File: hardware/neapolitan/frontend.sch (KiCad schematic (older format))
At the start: 144 parts, among them J10 GND_CLIP, J2 RF-SHIELD-FRAME, J3 RF-SHIELD-COVER, J4 MOUNTING_HOLE, J5 MOUNTING_HOLE, J6 MOUNTING_HOLE, J7 MOUNTING_HOLE, J8 MOUNTING_HOLE, J9 MOUNTING_HOLE, P13 GPO1, P17 GPO6, P19 GPO3, P21 REF_IN, P27 MIXER_SDATA, P31 MIXER_SCLK, P32 MIXER_ENX, P33 MIXER_RESETX, P34 MIX_BYPASS, P35 !MIX_BYPASS, P4 ANTENNA, P42 TX, P43 RX, P44 HP, P45 LP, P46 TX_MIX_BP, P47 RX_MIX_BP, P48 TX_AMP, P49 RX_AMP, P50 AMP_BYPASS, P51 !TX_AMP_PWR, P52 !RX_AMP_PWR, P6 GPO4, P7 GPO2, Q1 MOSFET_P, Q2 MOSFET_P, Q4 MOSFET_P, T1 MIX_IN_BALUN, T2 MIX_OUT_BALUN, U1 SKY13350, U10 SKY13350, U11 SKY13350, U12 SKY13317, U13 MGA-81563, U14 SKY13317, U2 SKY13350, U25 MGA-81563, U3 RX_LOWPASS_FILTER, U4 RFFC5072, U5 SKY13350, U6 SKY13350, U7 SKY13350, U8 RX_HIGHPASS_FILTER, U9 SKY13317

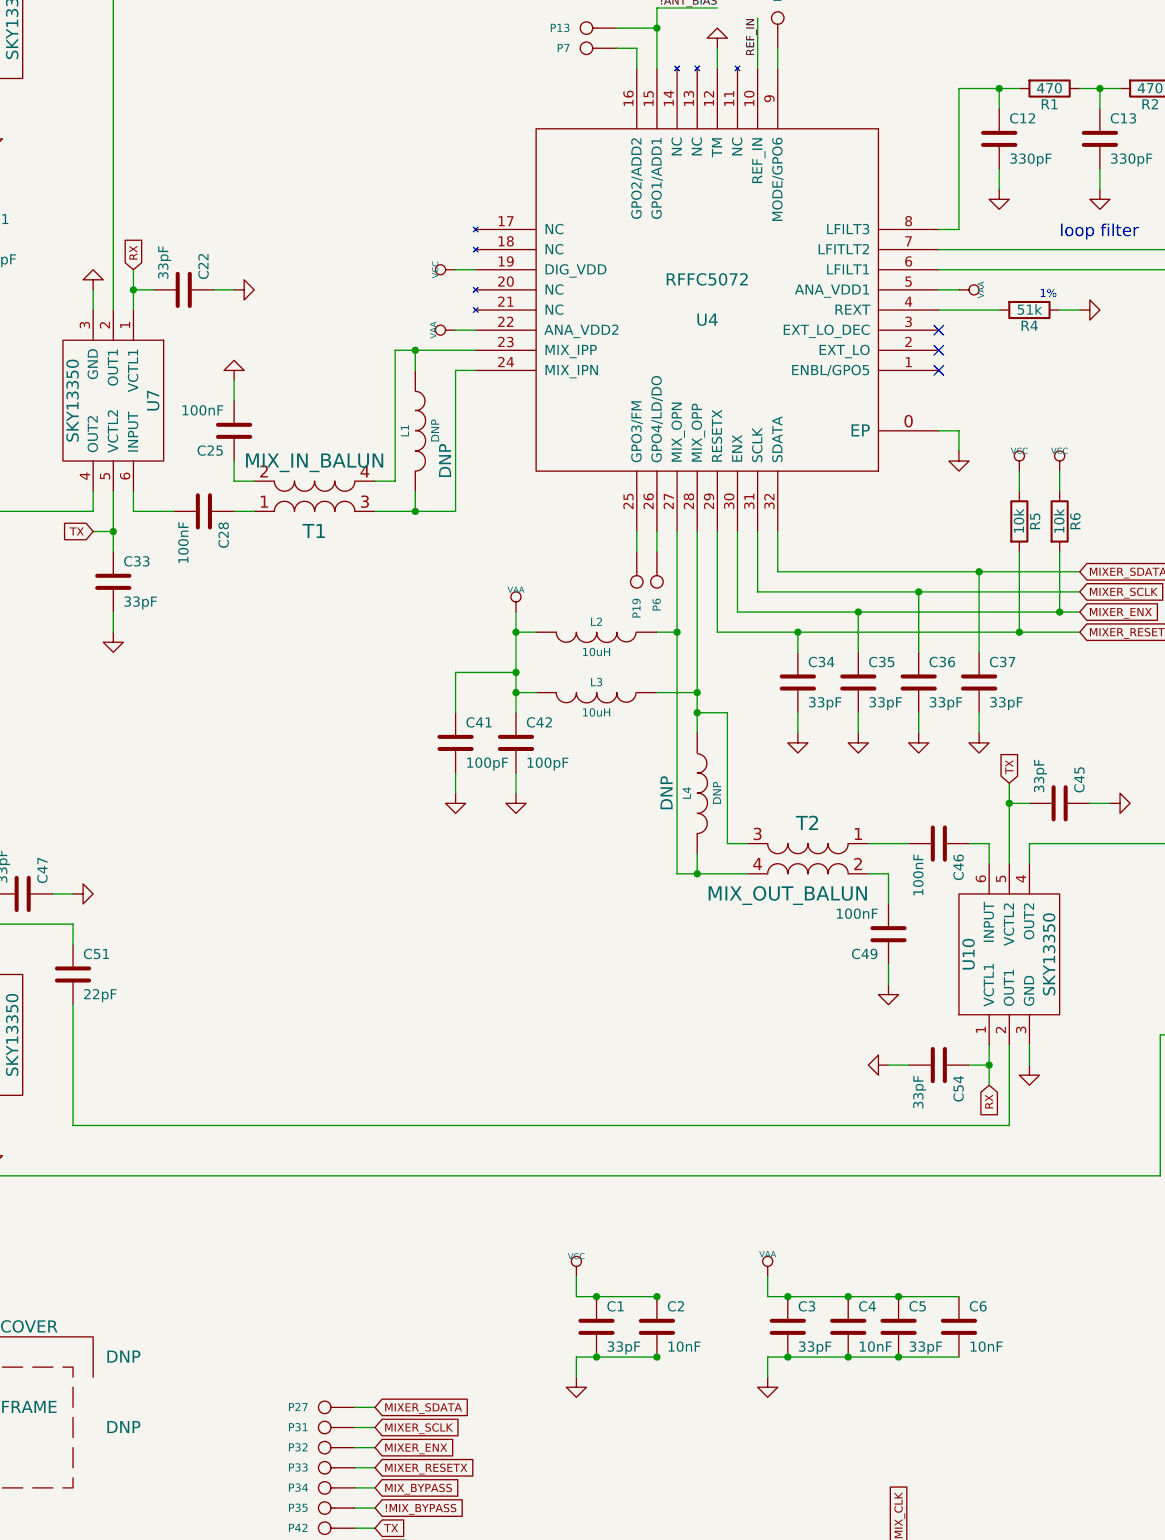
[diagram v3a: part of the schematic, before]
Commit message: Neapolitan: added RF chokes to some supply pins as a noise reduction experiment
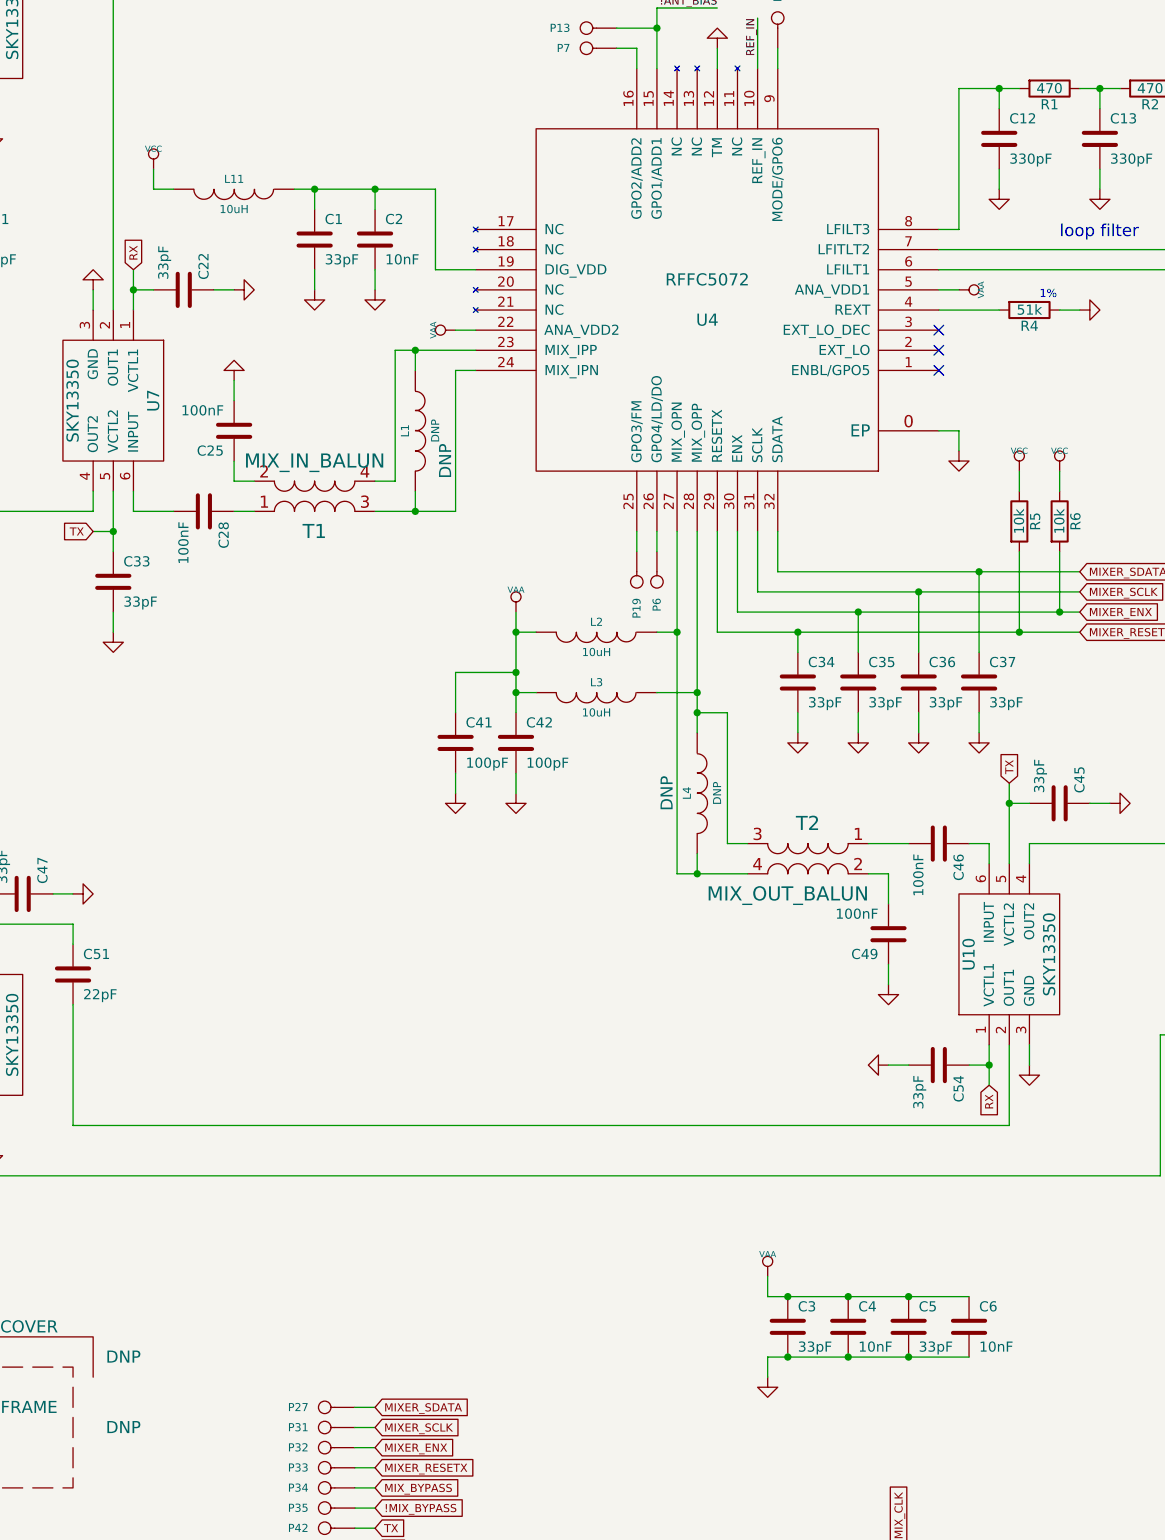
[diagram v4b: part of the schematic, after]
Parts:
- added L11: 10uH, hackrf:GSG-0603, symbol INDUCTOR
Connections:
- net VCC: now also L11.2; no longer C1.1, C2.1, U4.19 (DIG_VDD)
- new net: C1.1, C2.1, L11.1, U4.19 (DIG_VDD)
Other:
- moved on the sheet: C1, C2, C5, C6

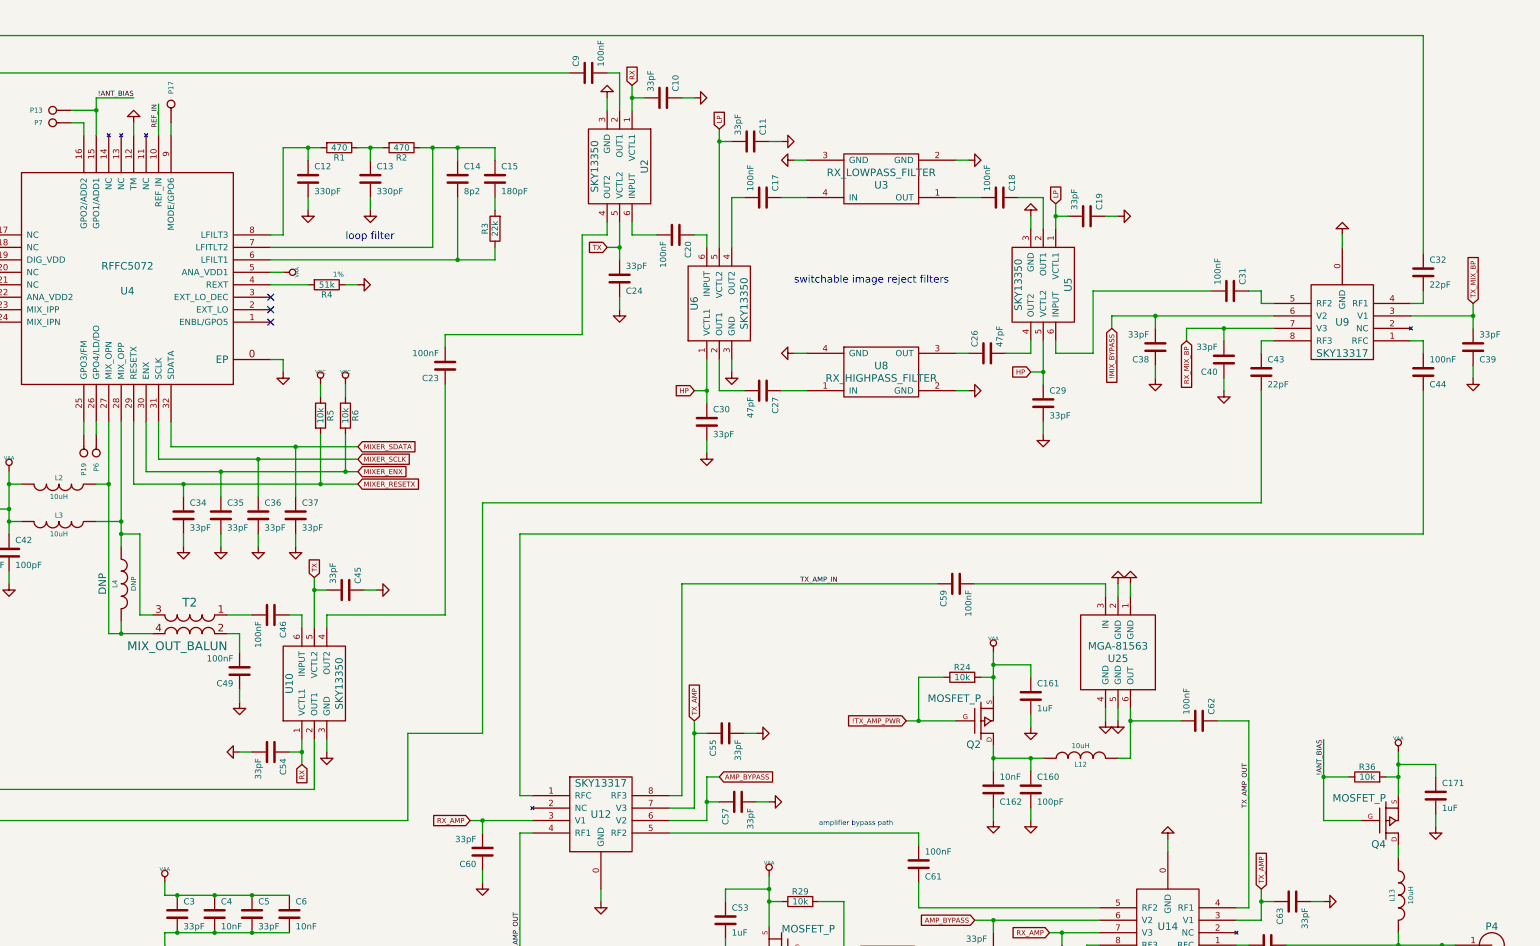
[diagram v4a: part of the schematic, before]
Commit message: Neapolitan: replaced antenna port power MOSFET with current limited power switch
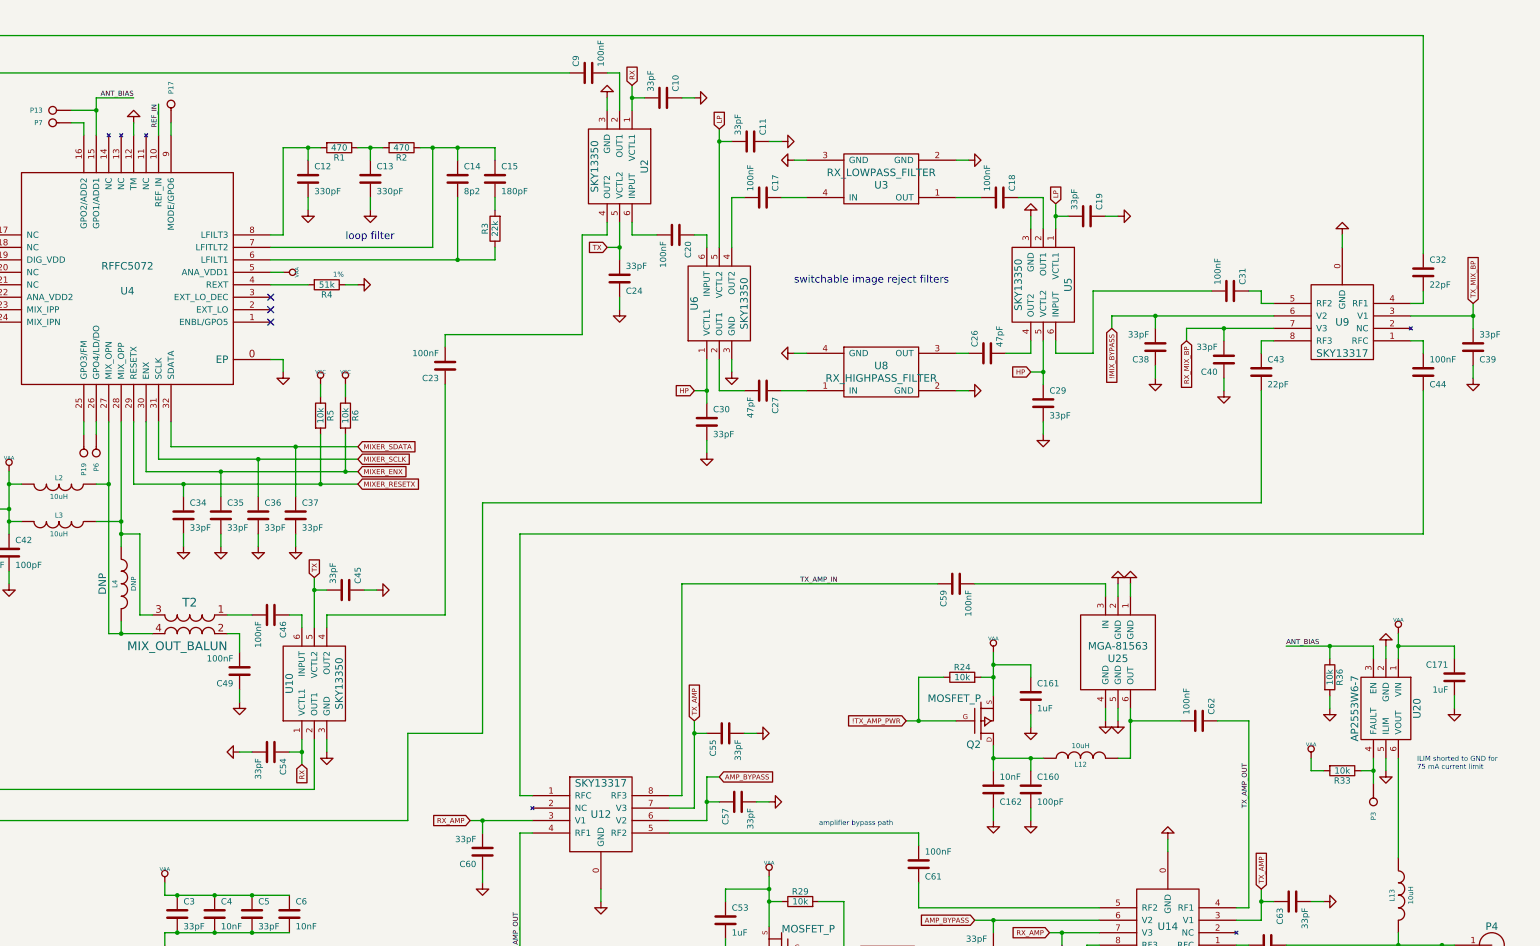
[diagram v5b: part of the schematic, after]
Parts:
- removed Q4: MOSFET_P, gsg-modules:SOT23GDS, symbol MOSFET_P
- added P3: ANT_FAULT, hackrf:GSG-TESTPOINT-50MIL, symbol CONN_1
- added R33: 10k, hackrf:GSG-0402, symbol R
- added U20: AP2553W6-7, gsg-modules:SOT457, symbol NX5P2553GV
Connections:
- net GND: now also R36.2, U20.2 (GND), U20.5 (ILIM)
- net VAA: now also R33.2, U20.1 (VIN); no longer R36.2
- net at L13.1: now also U20.6 (VOUT)
- net !ANT_BIAS renamed ANT_BIAS
- net ANT_BIAS: now also U20.3 (EN)
- new net: P3.1, R33.1, U20.4 (FAULT)
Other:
- note added: "ILIM shorted to GND for\n75 mA current limit"
- moved on the sheet: C171, R36
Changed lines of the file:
@@
 Wire Wire Line
 	16300 8850 16300 8950
-Connection ~ 15550 7100
-Wire Wire Line
-	15550 7100 15450 7100
-Wire Wire Line
-	15850 7100 15850 7000
-Wire Wire Line
-	15850 7500 15850 7400
-Wire Wire Line
-	15550 6900 15550 7250
-Connection ~ 15550 7000
-Wire Wire Line
-	15150 7100 14950 7100
-Wire Wire Line
-	14950 6800 14950 7450
-Wire Wire Line
-	15850 7000 15550 7000
 $Comp
 L VAA #PWR089
 U 1 1 52EA1171
-P 15550 6900
-F 0 "#PWR089" H 15550 6960 30  0001 C CNN
-F 1 "VAA" H 15550 7010 30  0000 C CNN
-F 2 "" H 15550 6900 60  0001 C CNN
-F 3 "" H 15550 6900 60  0001 C CNN
-	1    15550 6900
+P 15550 5950
+F 0 "#PWR089" H 15550 6010 30  0001 C CNN
+F 1 "VAA" H 15550 6060 30  0000 C CNN
+F 2 "" H 15550 5950 60  0001 C CNN
+F 3 "" H 15550 5950 60  0001 C CNN
+	1    15550 5950
 	1    0    0    -1
 $EndComp
@@
 L GND #PWR090
 U 1 1 52EA1177
-P 15850 7500
-F 0 "#PWR090" H 15850 7500 30  0001 C CNN
-F 1 "GND" H 15850 7430 30  0001 C CNN
-F 2 "" H 15850 7500 60  0001 C CNN
-F 3 "" H 15850 7500 60  0001 C CNN
-	1    15850 7500
+P 16000 6550
+F 0 "#PWR090" H 16000 6550 30  0001 C CNN
+F 1 "GND" H 16000 6480 30  0001 C CNN
+F 2 "" H 16000 6550 60  0001 C CNN
+F 3 "" H 16000 6550 60  0001 C CNN
+	1    16000 6550
 	1    0    0    -1
 $EndComp
@@
 L R R36
 U 1 1 52EA1180
-P 15300 7100
-F 0 "R36" V 15380 7100 50  0000 C CNN
-F 1 "10k" V 15300 7100 50  0000 C CNN
-F 2 "hackrf:GSG-0402" H 15300 7100 60  0001 C CNN
-F 3 "" H 15300 7100 60  0001 C CNN
-F 4 "Stackpole" H 15300 7100 60  0001 C CNN "Manufacturer"
-F 5 "RMCF0402JT10K0" H 15300 7100 60  0001 C CNN "Part Number"
-F 6 "RES 10K OHM 1/16W 5% 0402 SMD" H 15300 7100 60  0001 C CNN "Description"
-	1    15300 7100
-	0    -1   -1   0
+P 15000 6300
+F 0 "R36" V 15080 6300 50  0000 C CNN
+F 1 "10k" V 15000 6300 50  0000 C CNN
+F 2 "hackrf:GSG-0402" H 15000 6300 60  0001 C CNN
+F 3 "" H 15000 6300 60  0001 C CNN
+F 4 "Stackpole" H 15000 6300 60  0001 C CNN "Manufacturer"
+F 5 "RMCF0402JT10K0" H 15000 6300 60  0001 C CNN "Part Number"
+F 6 "RES 10K OHM 1/16W 5% 0402 SMD" H 15000 6300 60  0001 C CNN "Description"
+	1    15000 6300
+	1    0    0    -1
 $EndComp
 $Comp
@@
 L C C171
 U 1 1 52EA119B
-P 15850 7250
-F 0 "C171" H 15900 7350 50  0000 L CNN
-F 1 "1uF" H 15900 7150 50  0000 L CNN
-F 2 "hackrf:GSG-0402" H 15850 7250 60  0001 C CNN
-F 3 "" H 15850 7250 60  0001 C CNN
-F 4 "Taiyo Yuden" H 15850 7250 60  0001 C CNN "Manufacturer"
-F 5 "LMK105BJ105KV-F" H 15850 7250 60  0001 C CNN "Part Number"
-F 6 "CAP CER 1UF 10V 10% X5R 0402" H 15850 7250 60  0001 C CNN "Description"
-	1    15850 7250
-	1    0    0    -1
-$EndComp
-$Comp
-L MOSFET_P Q4
-U 1 1 52EA11B0
-P 15450 7450
-F 0 "Q4" H 15450 7640 60  0000 R CNN
-F 1 "MOSFET_P" H 15450 7270 60  0000 R CNN
-F 2 "gsg-modules:SOT23GDS" H 15450 7450 60  0001 C CNN
-F 3 "" H 15450 7450 60  0001 C CNN
-F 4 "Fairchild" H 15450 7450 60  0001 C CNN "Manufacturer"
-F 5 "BSS84" H 15450 7450 60  0001 C CNN "Part Number"
-F 6 "MOSFET P-CH 50V 130MA SOT-23" H 15450 7450 60  0001 C CNN "Description"
-	1    15450 7450
-	1    0    0    1
+P 16000 6300
+F 0 "C171" H 16050 6400 50  0000 L CNN
+F 1 "1uF" H 16050 6200 50  0000 L CNN
+F 2 "hackrf:GSG-0402" H 16000 6300 60  0001 C CNN
+F 3 "" H 16000 6300 60  0001 C CNN
+F 4 "Taiyo Yuden" H 16000 6300 60  0001 C CNN "Manufacturer"
+F 5 "LMK105BJ105KV-F" H 16000 6300 60  0001 C CNN "Part Number"
+F 6 "CAP CER 1UF 10V 10% X5R 0402" H 16000 6300 60  0001 C CNN "Description"
+	1    16000 6300
+	-1   0    0    -1
 $EndComp
 Wire Wire Line
@@
 Connection ~ 15550 8450
 Wire Wire Line
-	14950 7450 15250 7450
-Connection ~ 14950 7100
-Wire Wire Line
-	15550 7650 15550 7750
+	15550 6950 15550 7750
 Wire Wire Line
 	5000 1850 4900 1850
@@
 Connection ~ 5100 1750
 Text Label 5400 1650 2    40   ~ 0
-!ANT_BIAS
+ANT_BIAS
 Wire Wire Line
 	5100 1650 5400 1650
-Text Label 14950 6800 3    40   ~ 0
-!ANT_BIAS
+Text Label 14650 6050 0    40   ~ 0
+ANT_BIAS
 Wire Wire Line
 	15650 3400 16150 3400
@@
 	4000 2950 4000 2550
 Connection ~ 3700 2550
+$Comp
+L NX5P2553GV U20
+U 1 1 57E6AE8D
+P 15450 6550
+F 0 "U20" H 15450 6800 60  0000 C CNN
+F 1 "AP2553W6-7" H 15450 6300 60  0000 C CNN
+F 2 "gsg-modules:SOT457" H 15450 6550 60  0001 C CNN
+F 3 "" H 15450 6550 60  0000 C CNN
+F 4 "Diodes Inc." H 15450 6550 60  0001 C CNN "Manufacturer"
+F 5 "AP2553W6-7" H 15450 6550 60  0001 C CNN "Part Number"
+F 6 "IC PD SW CURR LIMIT SOT26" H 15450 6550 60  0001 C CNN "Description"
+	1    15450 6550
+	0    1    1    0
+$EndComp
+$Comp
+L GND #PWR092
+U 1 1 57E6B2C6
+P 15450 6050
+F 0 "#PWR092" H 15450 6050 30  0001 C CNN
+F 1 "GND" H 15450 5980 30  0001 C CNN
+F 2 "" H 15450 6050 60  0001 C CNN
+F 3 "" H 15450 6050 60  0001 C CNN
+	1    15450 6050
+	-1   0    0    1
+$EndComp
+$Comp
+L GND #PWR093
+U 1 1 57E6CFB6
+P 15000 6550
+F 0 "#PWR093" H 15000 6550 30  0001 C CNN
+F 1 "GND" H 15000 6480 30  0001 C CNN
+F 2 "" H 15000 6550 60  0001 C CNN
+F 3 "" H 15000 6550 60  0001 C CNN
+	1    15000 6550
+	1    0    0    -1
+$EndComp
+Wire Wire Line
+	15000 6450 15000 6550
+Wire Wire Line
+	14650 6050 15350 6050
+Wire Wire Line
+	15000 6050 15000 6150
+Connection ~ 15000 6050
+$Comp
+L R R33
+U 1 1 57E6E64A
+P 15100 7050
+F 0 "R33" V 15180 7050 50  0000 C CNN
+F 1 "10k" V 15100 7050 50  0000 C CNN
+F 2 "hackrf:GSG-0402" H 15100 7050 60  0001 C CNN
+F 3 "" H 15100 7050 60  0001 C CNN
+F 4 "Stackpole" H 15100 7050 60  0001 C CNN "Manufacturer"
+F 5 "RMCF0402JT10K0" H 15100 7050 60  0001 C CNN "Part Number"
+F 6 "RES 10K OHM 1/16W 5% 0402 SMD" H 15100 7050 60  0001 C CNN "Description"
+	1    15100 7050
+	0    1    1    0
+$EndComp
+$Comp
+L GND #PWR094
+U 1 1 57E70C91
+P 15450 7050
+F 0 "#PWR094" H 15450 7050 30  0001 C CNN
+F 1 "GND" H 15450 6980 30  0001 C CNN
+F 2 "" H 15450 7050 60  0001 C CNN
+F 3 "" H 15450 7050 60  0001 C CNN
+	1    15450 7050
+	1    0    0    -1
+$EndComp
+Wire Wire Line
+	15450 7050 15450 6950
+Wire Wire Line
+	15550 5950 15550 6150
+Wire Wire Line
+	15550 6050 16000 6050
+Wire Wire Line
+	16000 6050 16000 6150
+Connection ~ 15550 6050
+Wire Wire Line
+	16000 6450 16000 6550
+Wire Wire Line
+	15450 6050 15450 6150
+Wire Wire Line
+	15350 6050 15350 6150
+$Comp
+L VAA #PWR095
+U 1 1 57E75398
+P 14850 6950
+F 0 "#PWR095" H 14850 7010 30  0001 C CNN
+F 1 "VAA" H 14850 7060 30  0000 C CNN
+F 2 "" H 14850 6950 60  0001 C CNN
+F 3 "" H 14850 6950 60  0001 C CNN
+	1    14850 6950
+	1    0    0    -1
+$EndComp
+Wire Wire Line
+	14850 6950 14850 7050
+Wire Wire Line
+	14850 7050 14950 7050
+Wire Wire Line
+	15250 7050 15350 7050
+Wire Wire Line
+	15350 6950 15350 7150
+$Comp
+L CONN_1 P3
+U 1 1 57E76694
+P 15350 7300
+F 0 "P3" H 15430 7300 40  0000 L CNN
+F 1 "ANT_FAULT" H 15350 7355 30  0001 C CNN
+F 2 "hackrf:GSG-TESTPOINT-50MIL" H 15350 7300 60  0001 C CNN
+F 3 "" H 15350 7300 60  0001 C CNN
+F 4 "DNP" H 15350 7300 60  0001 C CNN "Note"
+	1    15350 7300
+	0    1    1    0
+$EndComp
+Connection ~ 15350 7050
+Text Notes 15700 7050 0    40   ~ 0
+ILIM shorted to GND for\n75 mA current limit
 $EndSCHEMATC
